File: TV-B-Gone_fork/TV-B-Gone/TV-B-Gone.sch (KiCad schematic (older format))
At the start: 21 parts, among them J1 AVR-ISP-6, Q1 2N3904, Q2 2N3904, Q3 BC557, Q4 2N3904, Q5 2N3904, U1 ATtiny85V-10PU, Y1 8Mhz

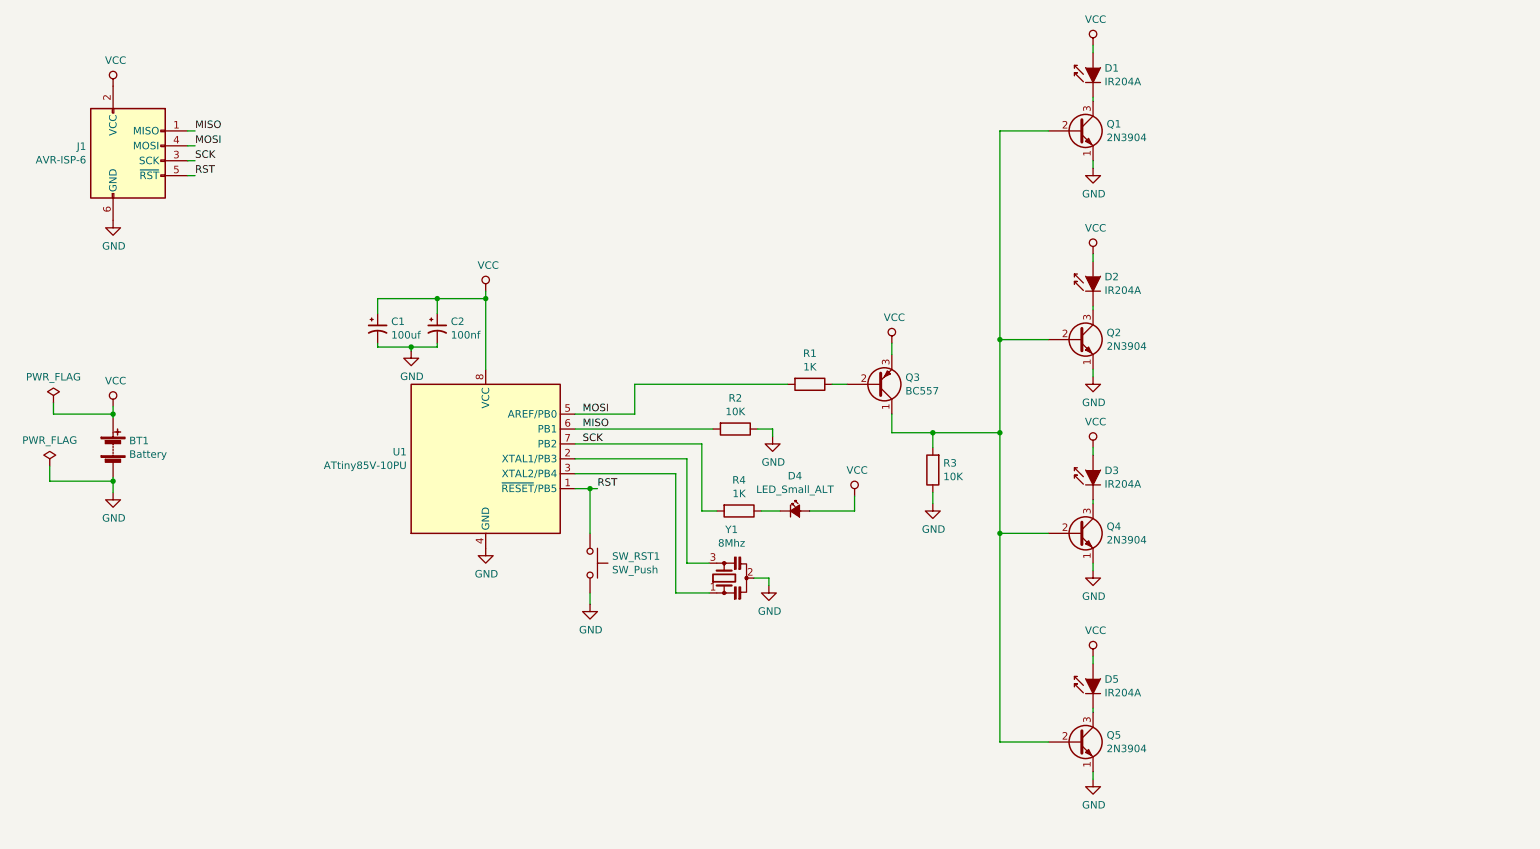
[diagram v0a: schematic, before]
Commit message: Agregado capacitores para optar entre resonador o cristal.
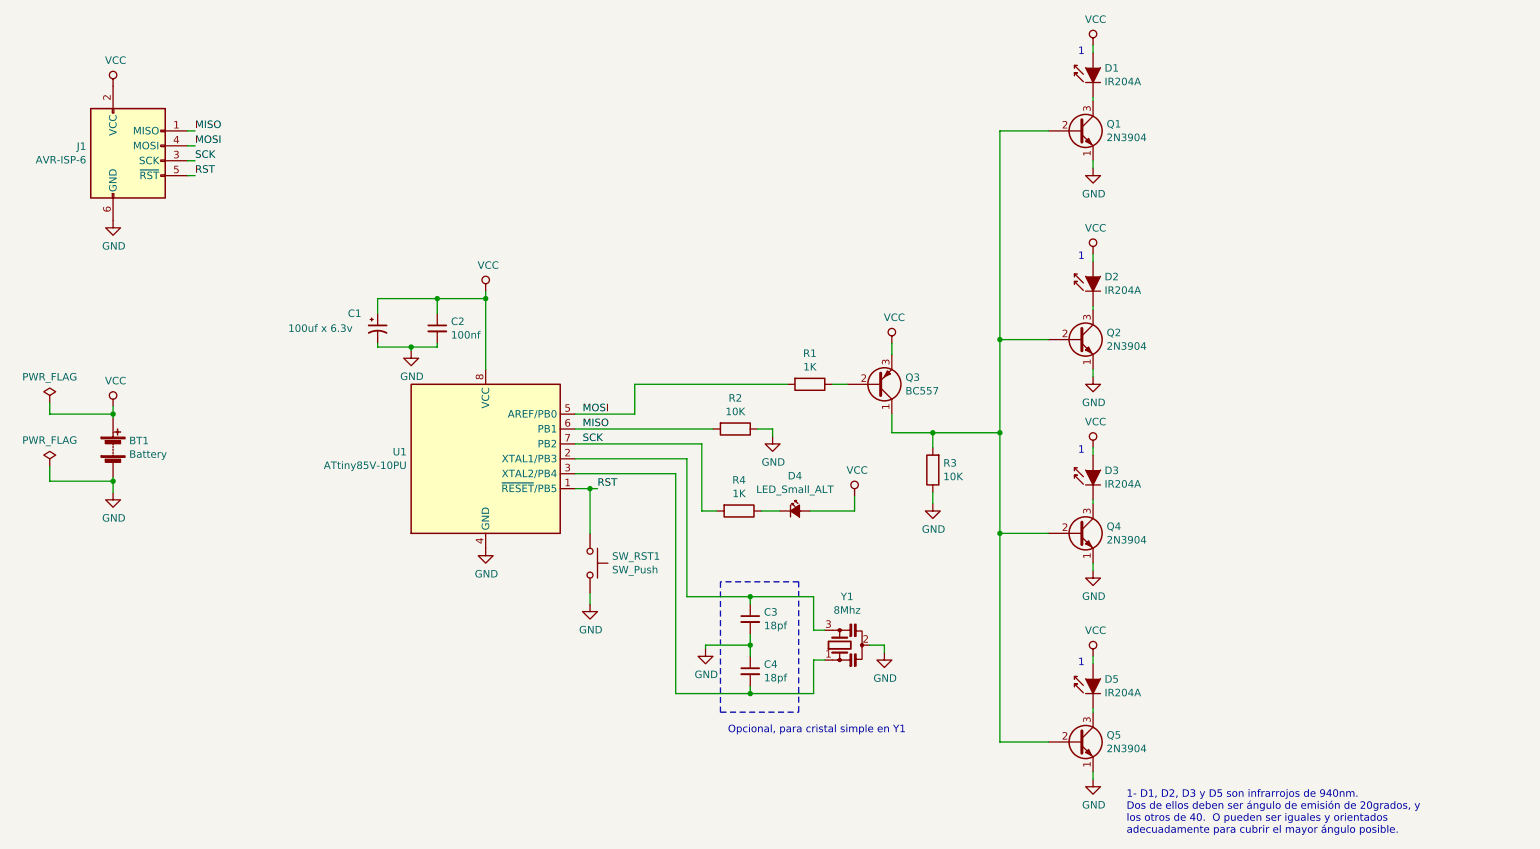
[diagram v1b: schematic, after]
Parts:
- removed C2: 100nf, Capacitor_THT:C_Disc_D6.0mm_W2.5mm_P5.00mm, symbol Device:CP1_Small
- added C2: 100nf, Capacitor_THT:C_Disc_D7.5mm_W2.5mm_P5.00mm, symbol Device:C_Small
- added C3, C4: 18pf, Capacitor_THT:C_Disc_D3.0mm_W2.0mm_P2.50mm, symbol Device:C_Small
- C1: value 100uf -> 100uf x 6.3v
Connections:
- net GND: now also C2.2, C3.2, C4.1
- net VCC: now also C2.1
- net at U1.2 (XTAL1/PB3), Y1.3: now also C3.1
- net at U1.3 (XTAL2/PB4), Y1.1: now also C4.2
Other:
- note added: "1"
- note added: "1- D1, D2, D3 y D5 son infrarrojos de 940nm.\nDos de ellos deben ser ángulo de emisión de 20grados, y \nlos otros de 40. O pueden ser iguales y orientados\nadecuadamente para cubrir el mayor ángulo posible."
- note added: "Opcional, para cristal simple en Y1"
- moved on the sheet: Y1
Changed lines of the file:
@@
 EESchema Schematic File Version 4
+LIBS:TV-B-Gone-cache
 EELAYER 26 0
 EELAYER END
@@
 L power:GND #PWR018
 U 1 1 5D984E97
-P 6500 4650
-F 0 "#PWR018" H 6500 4400 50  0001 C CNN
-F 1 "GND" H 6505 4477 50  0000 C CNN
-F 2 "" H 6500 4650 50  0001 C CNN
-F 3 "" H 6500 4650 50  0001 C CNN
-	1    6500 4650
+P 7275 5100
+F 0 "#PWR018" H 7275 4850 50  0001 C CNN
+F 1 "GND" H 7280 4927 50  0000 C CNN
+F 2 "" H 7275 5100 50  0001 C CNN
+F 3 "" H 7275 5100 50  0001 C CNN
+	1    7275 5100
 	1    0    0    -1
 $EndComp
@@
 $EndComp
 $Comp
-L Device:CP1_Small C2
-U 1 1 5D985158
-P 4275 2925
-F 0 "C2" H 4366 2971 50  0000 L CNN
-F 1 "100nf" H 4366 2880 50  0000 L CNN
-F 2 "Capacitor_THT:C_Disc_D6.0mm_W2.5mm_P5.00mm" H 4275 2925 50  0001 C CNN
-F 3 "~" H 4275 2925 50  0001 C CNN
-	1    4275 2925
-	1    0    0    -1
-$EndComp
-$Comp
 L Device:CP1_Small C1
 U 1 1 5D98525C
 P 3875 2925
-F 0 "C1" H 3966 2971 50  0000 L CNN
-F 1 "100uf" H 3966 2880 50  0000 L CNN
+F 0 "C1" H 3675 3025 50  0000 L CNN
+F 1 "100uf x 6.3v" H 3275 2925 50  0000 L CNN
 F 2 "Capacitor_THT:CP_Radial_D6.3mm_P2.50mm" H 3875 2925 50  0001 C CNN
 F 3 "~" H 3875 2925 50  0001 C CNN
@@
 L Device:Resonator_Small Y1
 U 1 1 5D985FD1
-P 6200 4600
-F 0 "Y1" V 6525 4550 50  0000 C CNN
-F 1 "8Mhz" V 6434 4550 50  0000 C CNN
-F 2 "Crystal:Resonator-3Pin_W10.0mm_H5.0mm" H 6175 4600 50  0001 C CNN
-F 3 "~" H 6175 4600 50  0001 C CNN
-	1    6200 4600
+P 6975 5050
+F 0 "Y1" V 7300 5000 50  0000 C CNN
+F 1 "8Mhz" V 7209 5000 50  0000 C CNN
+F 2 "Crystal:Resonator-3Pin_W10.0mm_H5.0mm" H 6950 5050 50  0001 C CNN
+F 3 "~" H 6950 5050 50  0001 C CNN
+	1    6975 5050
 	0    -1   -1   0
 $EndComp
@@
 	5200 3800 5950 3800
 Wire Wire Line
-	5950 3800 5950 4500
-Wire Wire Line
-	5950 4500 6100 4500
-Wire Wire Line
-	6100 4700 5875 4700
-Wire Wire Line
-	5875 4700 5875 3900
+	5950 3800 5950 4725
+Wire Wire Line
+	5950 4725 6375 4725
+Wire Wire Line
+	6800 5375 6375 5375
+Wire Wire Line
+	5875 5375 5875 3900
 Wire Wire Line
 	5875 3900 5200 3900
 Wire Wire Line
-	6400 4600 6500 4600
-Wire Wire Line
-	6500 4600 6500 4650
+	7175 5050 7275 5050
+Wire Wire Line
+	7275 5050 7275 5100
 $Comp
 L Transistor_BJT:2N3904 Q1
@@
 L power:PWR_FLAG #FLG0101
 U 1 1 5D9A5D91
-P 1700 3425
-F 0 "#FLG0101" H 1700 3500 50  0001 C CNN
-F 1 "PWR_FLAG" H 1700 3599 50  0000 C CNN
-F 2 "" H 1700 3425 50  0001 C CNN
-F 3 "~" H 1700 3425 50  0001 C CNN
-	1    1700 3425
+P 1675 3425
+F 0 "#FLG0101" H 1675 3500 50  0001 C CNN
+F 1 "PWR_FLAG" H 1675 3599 50  0000 C CNN
+F 2 "" H 1675 3425 50  0001 C CNN
+F 3 "~" H 1675 3425 50  0001 C CNN
+	1    1675 3425
 	1    0    0    -1
 $EndComp
@@
 $EndComp
 Wire Wire Line
-	1700 3425 1700 3500
-Wire Wire Line
-	1700 3500 2100 3500
+	1675 3425 1675 3500
+Wire Wire Line
+	1675 3500 2100 3500
 Connection ~ 2100 3500
 Wire Wire Line
@@
 Wire Wire Line
 	2100 3950 2100 4025
+$Comp
+L Device:C_Small C3
+U 1 1 5D994F2F
+P 6375 4875
+F 0 "C3" H 6467 4921 50  0000 L CNN
+F 1 "18pf" H 6467 4830 50  0000 L CNN
+F 2 "Capacitor_THT:C_Disc_D3.0mm_W2.0mm_P2.50mm" H 6375 4875 50  0001 C CNN
+F 3 "~" H 6375 4875 50  0001 C CNN
+	1    6375 4875
+	1    0    0    -1
+$EndComp
+$Comp
+L Device:C_Small C4
+U 1 1 5D996684
+P 6375 5225
+F 0 "C4" H 6467 5271 50  0000 L CNN
+F 1 "18pf" H 6467 5180 50  0000 L CNN
+F 2 "Capacitor_THT:C_Disc_D3.0mm_W2.0mm_P2.50mm" H 6375 5225 50  0001 C CNN
+F 3 "~" H 6375 5225 50  0001 C CNN
+	1    6375 5225
+	1    0    0    -1
+$EndComp
+Wire Wire Line
+	6800 4725 6800 4950
+Wire Wire Line
+	6800 4950 6875 4950
+Wire Wire Line
+	6875 5150 6800 5150
+Wire Wire Line
+	6800 5150 6800 5375
+$Comp
+L power:GND #PWR022
+U 1 1 5D99C614
+P 6075 5075
+F 0 "#PWR022" H 6075 4825 50  0001 C CNN
+F 1 "GND" H 6080 4902 50  0000 C CNN
+F 2 "" H 6075 5075 50  0001 C CNN
+F 3 "" H 6075 5075 50  0001 C CNN
+	1    6075 5075
+	1    0    0    -1
+$EndComp
+Wire Wire Line
+	6375 4775 6375 4725
+Connection ~ 6375 4725
+Wire Wire Line
+	6375 4725 6800 4725
+Wire Wire Line
+	6375 4975 6375 5050
+Wire Wire Line
+	6375 5325 6375 5375
+Connection ~ 6375 5375
+Wire Wire Line
+	6375 5375 5875 5375
+Wire Wire Line
+	6075 5075 6075 5050
+Wire Wire Line
+	6075 5050 6375 5050
+Connection ~ 6375 5050
+Wire Wire Line
+	6375 5050 6375 5125
+Wire Notes Line
+	6175 4625 6175 5500
+Wire Notes Line
+	6175 5500 6700 5500
+Wire Notes Line
+	6700 5500 6700 4625
+Wire Notes Line
+	6700 4625 6175 4625
+Text Notes 6225 5650 0    50   ~ 0
+Opcional, para cristal simple en Y1
+$Comp
+L Device:C_Small C2
+U 1 1 5D9AB272
+P 4275 2925
+F 0 "C2" H 4367 2971 50  0000 L CNN
+F 1 "100nf" H 4367 2880 50  0000 L CNN
+F 2 "Capacitor_THT:C_Disc_D7.5mm_W2.5mm_P5.00mm" H 4275 2925 50  0001 C CNN
+F 3 "~" H 4275 2925 50  0001 C CNN
+	1    4275 2925
+	1    0    0    -1
+$EndComp
+Text Notes 8575 1100 0    50   ~ 0
+1
+Text Notes 8575 2475 0    50   ~ 0
+1
+Text Notes 8575 3775 0    50   ~ 0
+1
+Text Notes 8575 5200 0    50   ~ 0
+1
+Text Notes 8900 6325 0    50   ~ 0
+1- D1, D2, D3 y D5 son infrarrojos de 940nm.\nDos de ellos deben ser ángulo de emisión de 20grados, y \nlos otros de 40.  O pueden ser iguales y orientados\nadecuadamente para cubrir el mayor ángulo posible.
 $EndSCHEMATC
